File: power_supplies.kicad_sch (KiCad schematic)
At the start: 0 parts

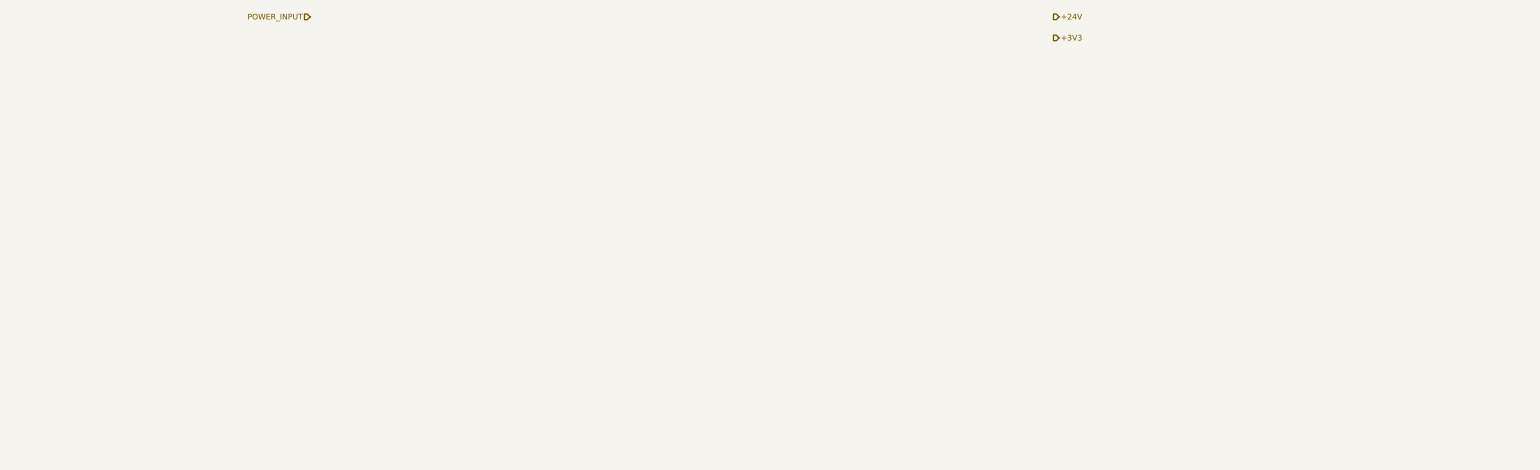
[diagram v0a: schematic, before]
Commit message: Add power stages
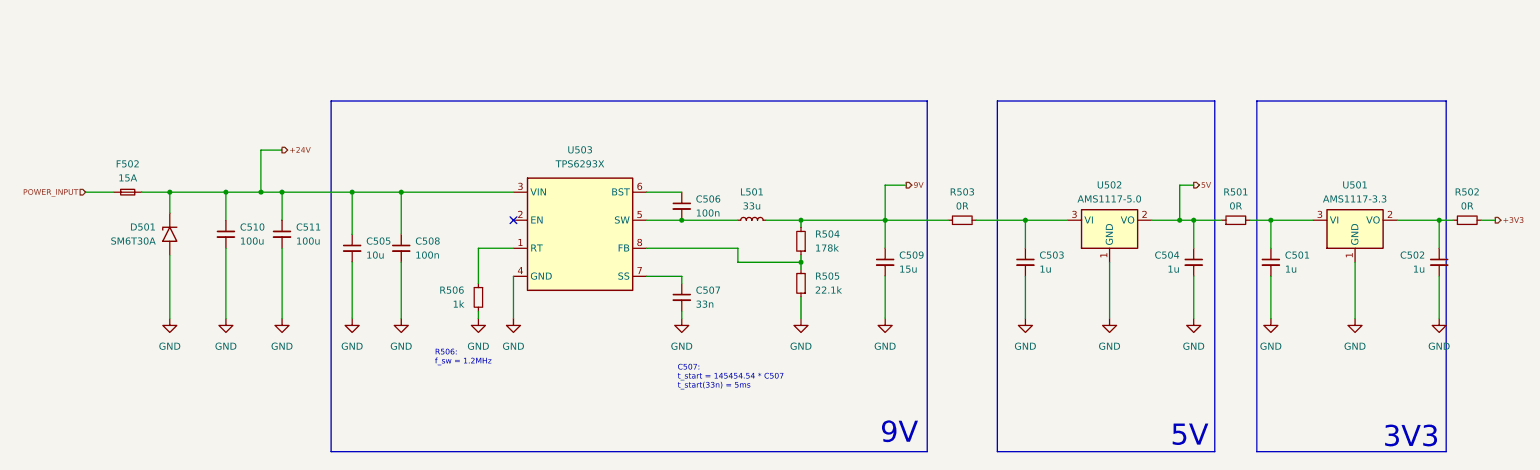
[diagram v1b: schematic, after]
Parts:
- added C501, C502, C503, C504: 1u, symbol Device:C_Small
- added C505: 10u, symbol Device:C_Small
- added C506, C508: 100n, symbol Device:C_Small
- added C507: 33n, symbol Device:C_Small
- added C509: 15u, symbol Device:C_Small
- added C510, C511: 100u, symbol Device:C_Small
- added D501: SM6T30A, Diode_SMD:D_SMB, symbol Diode:SM6T30A
- added F502: 15A, symbol Device:Fuse_Small
- added L501: 33u, symbol Device:L_Small
- added R501, R502, R503: 0R, symbol Device:R_Small
- added R504: 178k, symbol Device:R_Small
- added R505: 22.1k, symbol Device:R_Small
- added R506: 1k, symbol Device:R_Small
- added U501: AMS1117-3.3, Package_TO_SOT_SMD:SOT-223-3_TabPin2, symbol Regulator_Linear:AMS1117-3.3
- added U502: AMS1117-5.0, Package_TO_SOT_SMD:SOT-223-3_TabPin2, symbol Regulator_Linear:AMS1117-5.0
- added U503: TPS6293X, Package_TO_SOT_SMD:SOT-583-8, symbol Bond_Kicad_Lib:BD_TPS6293X
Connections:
- net +24V: now also C505.1, C508.1, C510.1, C511.1, D501.1 (A1), F502.2, U503.3 (VIN)
- net +3V3: now also R502.2
- net POWER_INPUT: now also F502.1
- new net: C503.1, R503.2, U502.3 (VI)
- new net: C506.2, L501.1, U503.5 (SW)
- new net: R506.1, U503.1 (RT)
- new net: C501.1, R501.2, U501.3 (VI)
- new net: C506.1, U503.6 (BST)
- new net: C507.1, U503.7 (SS)
- new net: R504.1, R505.2, U503.8 (FB)
- new net: C502.1, R502.1, U501.2 (VO)
- new net 5V: C504.1, R501.1, U502.2 (VO)
- new net 9V: C509.1, L501.2, R503.1, R504.2
- new net GND: C501.2, C502.2, C503.2, C504.2, C505.2, C507.2, C508.2, C509.2, C510.2, C511.2, D501.2 (A2), R505.1, R506.2, U501.1 (GND), U502.1 (GND), U503.4 (GND)
- no-connect marks 0 -> 1
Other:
- note added: "3V3"
- note added: "5V"
- note added: "9V"
- note added: "C507: t_start = 145454.54 * C507 t_start(33n) = 5ms"
- note added: "R506: f_sw = 1.2MHz"

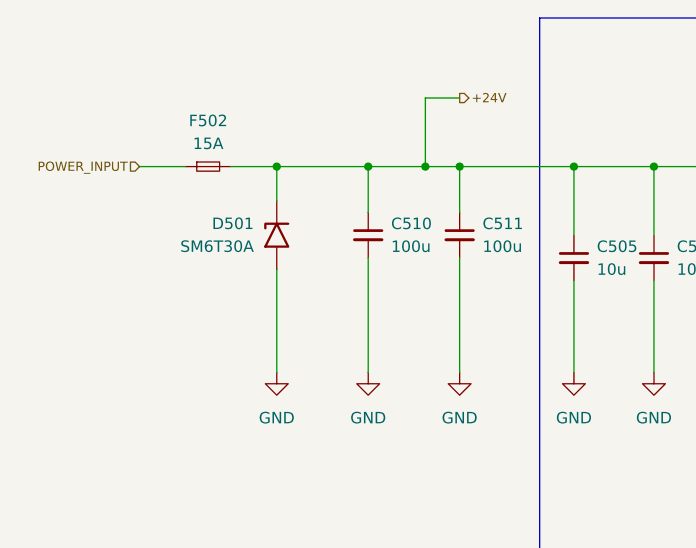
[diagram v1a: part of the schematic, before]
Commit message: Add power supplies
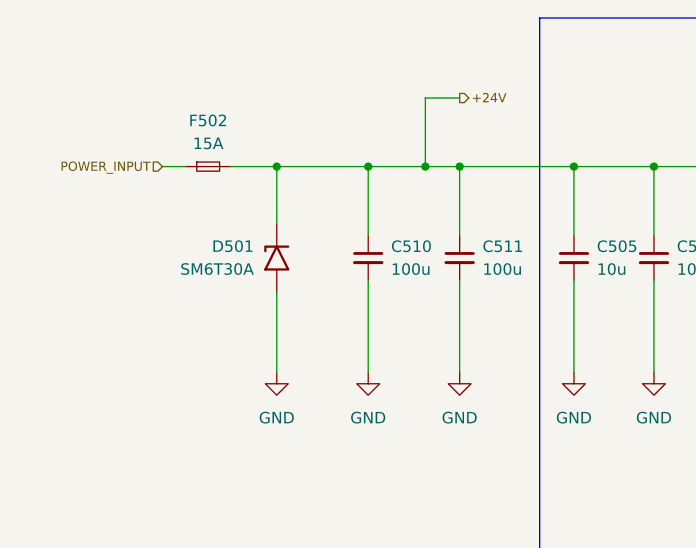
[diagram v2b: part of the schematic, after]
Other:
- moved on the sheet: C510, C511, D501
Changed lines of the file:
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@@
 	(wire
 		(pts
-			(xy 49.53 95.25) (xy 49.53 107.95)
+			(xy 49.53 97.79) (xy 49.53 107.95)
 		)
 		(stroke
@@
 	(wire
 		(pts
-			(xy 24.13 85.09) (xy 29.21 85.09)
+			(xy 26.67 85.09) (xy 29.21 85.09)
 		)
 		(stroke
@@
 	(wire
 		(pts
-			(xy 39.37 96.52) (xy 39.37 107.95)
+			(xy 39.37 99.06) (xy 39.37 107.95)
 		)
 		(stroke
@@
 	(wire
 		(pts
-			(xy 39.37 85.09) (xy 39.37 88.9)
+			(xy 39.37 85.09) (xy 39.37 91.44)
 		)
 		(stroke
@@
 	(wire
 		(pts
-			(xy 59.69 95.25) (xy 59.69 107.95)
+			(xy 59.69 97.79) (xy 59.69 107.95)
 		)
 		(stroke
@@
 	(wire
 		(pts
-			(xy 49.53 85.09) (xy 49.53 90.17)
+			(xy 49.53 85.09) (xy 49.53 92.71)
 		)
 		(stroke
@@
 	(wire
 		(pts
-			(xy 59.69 85.09) (xy 59.69 90.17)
+			(xy 59.69 85.09) (xy 59.69 92.71)
 		)
 		(stroke
@@
 	(hierarchical_label "POWER_INPUT"
 		(shape input)
-		(at 24.13 85.09 180)
+		(at 26.67 85.09 180)
 		(effects
 			(font
@@
 	(symbol
 		(lib_id "Device:C_Small")
-		(at 59.69 92.71 0)
+		(at 59.69 95.25 0)
 		(mirror y)
 		(unit 1)
@@
 		(fields_autoplaced yes)
 		(property "Reference" "C511"
-			(at 62.23 91.4462 0)
+			(at 62.23 93.9862 0)
 			(effects
 				(font
@@
 		)
 		(property "Value" "100u"
-			(at 62.23 93.9862 0)
+			(at 62.23 96.5262 0)
 			(effects
 				(font
@@
 		)
 		(property "Footprint" ""
-			(at 59.69 92.71 0)
+			(at 59.69 95.25 0)
 			(effects
 				(font
@@
 		)
 		(property "Datasheet" "~"
-			(at 59.69 92.71 0)
+			(at 59.69 95.25 0)
 			(effects
 				(font
@@
 		)
 		(property "Description" "Unpolarized capacitor, small symbol"
-			(at 59.69 92.71 0)
+			(at 59.69 95.25 0)
 			(effects
 				(font
@@
 	(symbol
 		(lib_id "Diode:SM6T30A")
-		(at 39.37 92.71 90)
+		(at 39.37 95.25 90)
 		(mirror x)
 		(unit 1)
@@
 		(fields_autoplaced yes)
 		(property "Reference" "D501"
-			(at 36.83 91.4399 90)
+			(at 36.83 93.9799 90)
 			(effects
 				(font
@@
 		)
 		(property "Value" "SM6T30A"
-			(at 36.83 93.9799 90)
+			(at 36.83 96.5199 90)
 			(effects
 				(font
@@
 		)
 		(property "Footprint" "Diode_SMD:D_SMB"
-			(at 44.45 92.71 0)
+			(at 44.45 95.25 0)
 			(effects
 				(font
@@
 		)
 		(property "Datasheet" "https://www.st.com/resource/en/datasheet/sm6t.pdf"
-			(at 39.37 91.44 0)
+			(at 39.37 93.98 0)
 			(effects
 				(font
@@
 		)
 		(property "Description" "600W unidirectional Transil Transient Voltage Suppressor, 30Vrwm, DO-214AA"
-			(at 39.37 92.71 0)
+			(at 39.37 95.25 0)
 			(effects
 				(font
@@
 	(symbol
 		(lib_id "Device:C_Small")
-		(at 49.53 92.71 0)
+		(at 49.53 95.25 0)
 		(mirror y)
 		(unit 1)
@@
 		(fields_autoplaced yes)
 		(property "Reference" "C510"
-			(at 52.07 91.4462 0)
+			(at 52.07 93.9862 0)
 			(effects
 				(font
@@
 		)
 		(property "Value" "100u"
-			(at 52.07 93.9862 0)
+			(at 52.07 96.5262 0)
 			(effects
 				(font
@@
 		)
 		(property "Footprint" ""
-			(at 49.53 92.71 0)
+			(at 49.53 95.25 0)
 			(effects
 				(font
@@
 		)
 		(property "Datasheet" "~"
-			(at 49.53 92.71 0)
+			(at 49.53 95.25 0)
 			(effects
 				(font
@@
 		)
 		(property "Description" "Unpolarized capacitor, small symbol"
-			(at 49.53 92.71 0)
-			(effects
-				(font
+			(at 49.53 95.25 0)
+			(effects
+				(font
